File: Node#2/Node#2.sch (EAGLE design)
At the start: 93 parts, among them IC1 TSL25911FN, J1 68712414522, Q1 BC847ALT1SMD, Q2 SI1308EDL-T1-GE3, U2 RV8564C3, U4 TPS63001DRCT

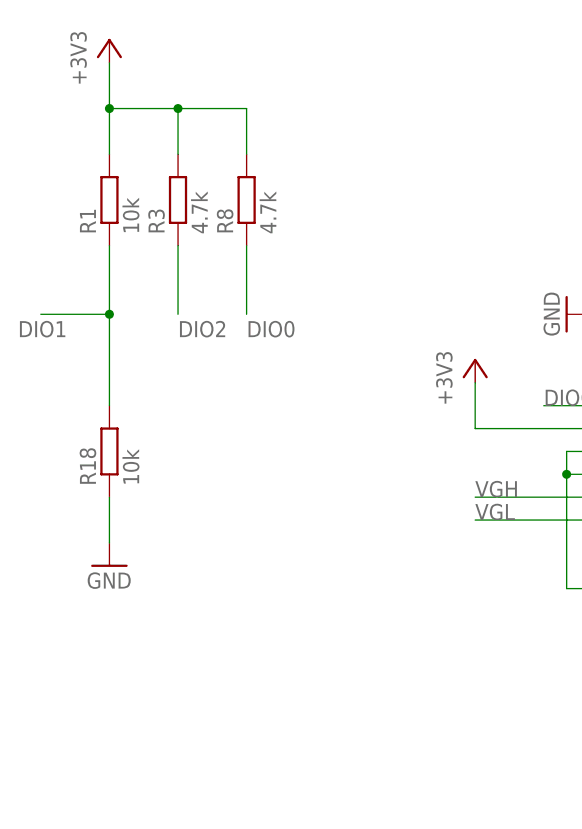
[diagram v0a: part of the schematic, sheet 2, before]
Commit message: Display gedreht, Diodenfootprints
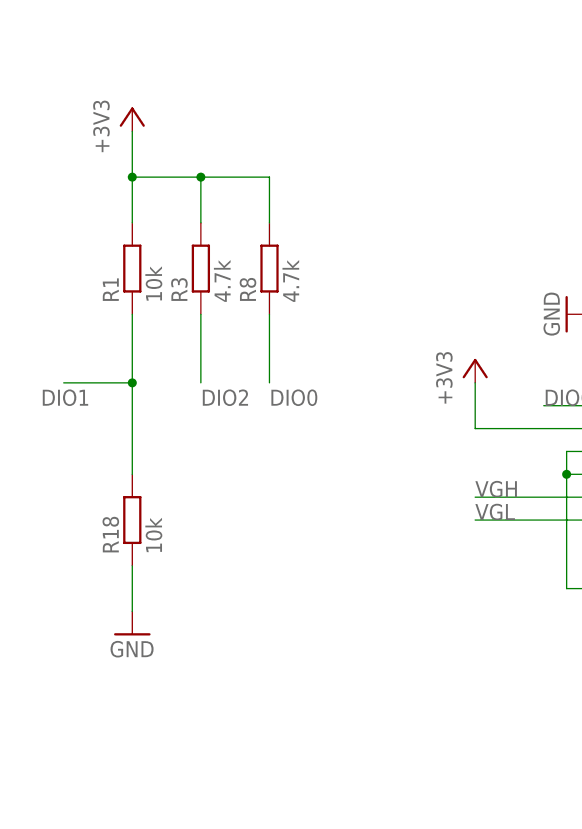
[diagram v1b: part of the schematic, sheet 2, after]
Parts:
- removed !!!FDN304PZ!!!: BSS84, transistor-small-signal:BSS84
- added Q3: FDN304PZ, BlueHome:FDN304PZ
- C1, C19, C2, C20, C21, C22, C23, C24, C25, C26, C27, C28, C29, C30: SPICEPREFIX (none) -> C
- C34: value (none) -> 100n
- D1: value ZPD -> ZENER_SMB; device diode:ZPD -> BlueHome:ZENER_SMB; SPICEPREFIX (none) -> D
- D2: value MUR150RL -> (none); device diode:MUR150RL -> eagle-ltspice:DIODE_E-
- D5, D6, D7: SPICEPREFIX (none) -> D
- J1, U$11: SPICEPREFIX (none) -> X
- Q2: SPICEPREFIX (none) -> Q
- R15, R16: SPICEPREFIX (none) -> R
- R17: value 1.5M -> 3M
- R5: value 1M -> 2M
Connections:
- removed net N$2: D2.A, R2.1
- new net N$1: D2.C, R2.1
- net +3V3_RTC: now also D2.A; no longer D2.C
- net N$14: now also Q3.G; no longer !!!FDN304PZ!!!.G
- net N$8: now also Q3.S; no longer !!!FDN304PZ!!!.S
- net N$9: now also Q3.D; no longer !!!FDN304PZ!!!.D
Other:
- moved on the sheet: R1, R18, R3, R8

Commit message: buttons
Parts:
- added ANT2: CONUFL001-SMD, BlueHome:CONUFL001-SMD
- added C53, C54, C55, C56, C57, C58, C59, C60, C61, C62: (no value), rcl:C-EUC0805K
- added C63, C64, C65, C66, C67, C68: (no value), rcl:C-EUC0805
- added C69, C70: (no value), rcl:C-EUC0402
- added D4: BAS40-06, diode:BAS40-06
- added JMP2: 0R-JUMPA, jump-0r-smd:0R-JUMPA
- added JP3: (no value), pinhead:PINHD-2X5
- added JP5: (no value), jumper:JP1E
- added JP7: (no value), pinhead:PINHD-1X3
- added JP8: (no value), pinhead:PINHD-1X2
- added R30, R31, R32, R33, R36, R37: (no value), rcl:R-EU_R0805
- added R34, R35: (no value), rcl:R-EU_R1210
- added S3, S4: FSM4JSMAATR, BlueHome:FSM4JSMAATR
- added U$15, U$17: L0402, BlueHome:L0402
- added U$16: BALF-NRG-01D3, BlueHome:BALF-NRG-01D3
- added U3: BLUENRG-232, BlueHome:BLUENRG-232
- added Y3: ECS-160-12-36-AGN-TR, BlueHome:ECS-160-12-36-AGN-TR
- added Y4: NX2012SA-32.768K-STD-MUB-1, BlueHome:NX2012SA-32.768K-STD-MUB-1
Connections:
- new net DIO14: C68.1, JP8.1, R34.1, S4.1, S4.2, U3.DIO14/ANATEST0
- new net JTCK: JP3.4, U3.DIO9
- new net JTMS: JP3.2, U3.DIO10
- new net N$47: C59.1, C60.1, U3.VDD1V2
- new net N$48: C61.1, C62.1, JMP2-0R.2, U3.SMPSFILT1
- new net N$49: R31.1, S3.1, S3.2
- new net N$50: C64.1, U3.FXTAL1, Y3.OUT/IN
- new net N$51: C65.2, U3.FXTAL0, Y3.IN/OUT
- new net N$52: C66.2, C67.2, U$15.1
- new net N$53: C66.1, U3.SXTAL0, Y4.2
- new net N$54: C67.1, U3.SXTAL1, Y4.1
- new net N$55: C69.1, U$16.ANT, U$17.1
- new net N$56: ANT2.SIG, C70.1, U$17.2
- new net N$57: JP3.1, JP5.1
- new net N$58: JP8.2, R35.2, S4.3, S4.4
- new net N$59: U$16.RX_P, U3.RF1
- new net N$60: U$16.RX_N, U3.RF0
- new net RXD: JP7.2, U3.DIO11
- new net SMPSFILT2: JMP2-0R.1, U3.SMPSFILT2
- new net TDI: JP3.8, R36.2, U3.DIO0
- new net TDO: JP3.6, R37.2, U3.DIO1
- new net TXD: JP7.1, U3.DIO8
- net +3V3: now also C53.1, C54.1, C55.1, C56.1, C57.1, C58.1, D4.K2, JMP2-0R.3, JP5.2, R30.2, R32.2, R33.2, R34.2, U3.VBAT1, U3.VBAT2, U3.VBAT3
- net ADC1: now also U3.ADC1
- net ADC2: now also U3.ADC2
- net DIO0: now also R36.1
- net DIO1: now also R37.1
- net DIO12: now also U3.DIO12
- net DIO13: now also U3.DIO13
- net DIO2: now also U3.DIO2
- net DIO3: now also U3.DIO3
- net DIO6: now also U3.DIO6
- net DIO7: now also U3.DIO7/BOOT
- net GND: now also ANT2.GND_1, ANT2.GND_2, C53.2, C54.2, C55.2, C56.2, C57.2, C58.2, C59.2, C60.2, C61.2, C62.2, C63.1, C64.2, C65.1, C68.2, C69.2, C70.2, JP3.3, JP3.5, JP3.9, JP7.3, R31.2, R35.1, U$15.2, U$16.GND, U3.EXP, U3.TEST, Y3.GND
- net RESETN: now also C63.2, D4.AA, JP3.10, R30.1, S3.3, S3.4, U3.RESETN
- net SCL: now also R32.1, U3.DIO4
- net SDA: now also R33.1, U3.DIO5
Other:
- note added: "9 IO"
- note added: "ARM 10-PIN Interface"
- note added: "JTAG"
- note added: "Serial"

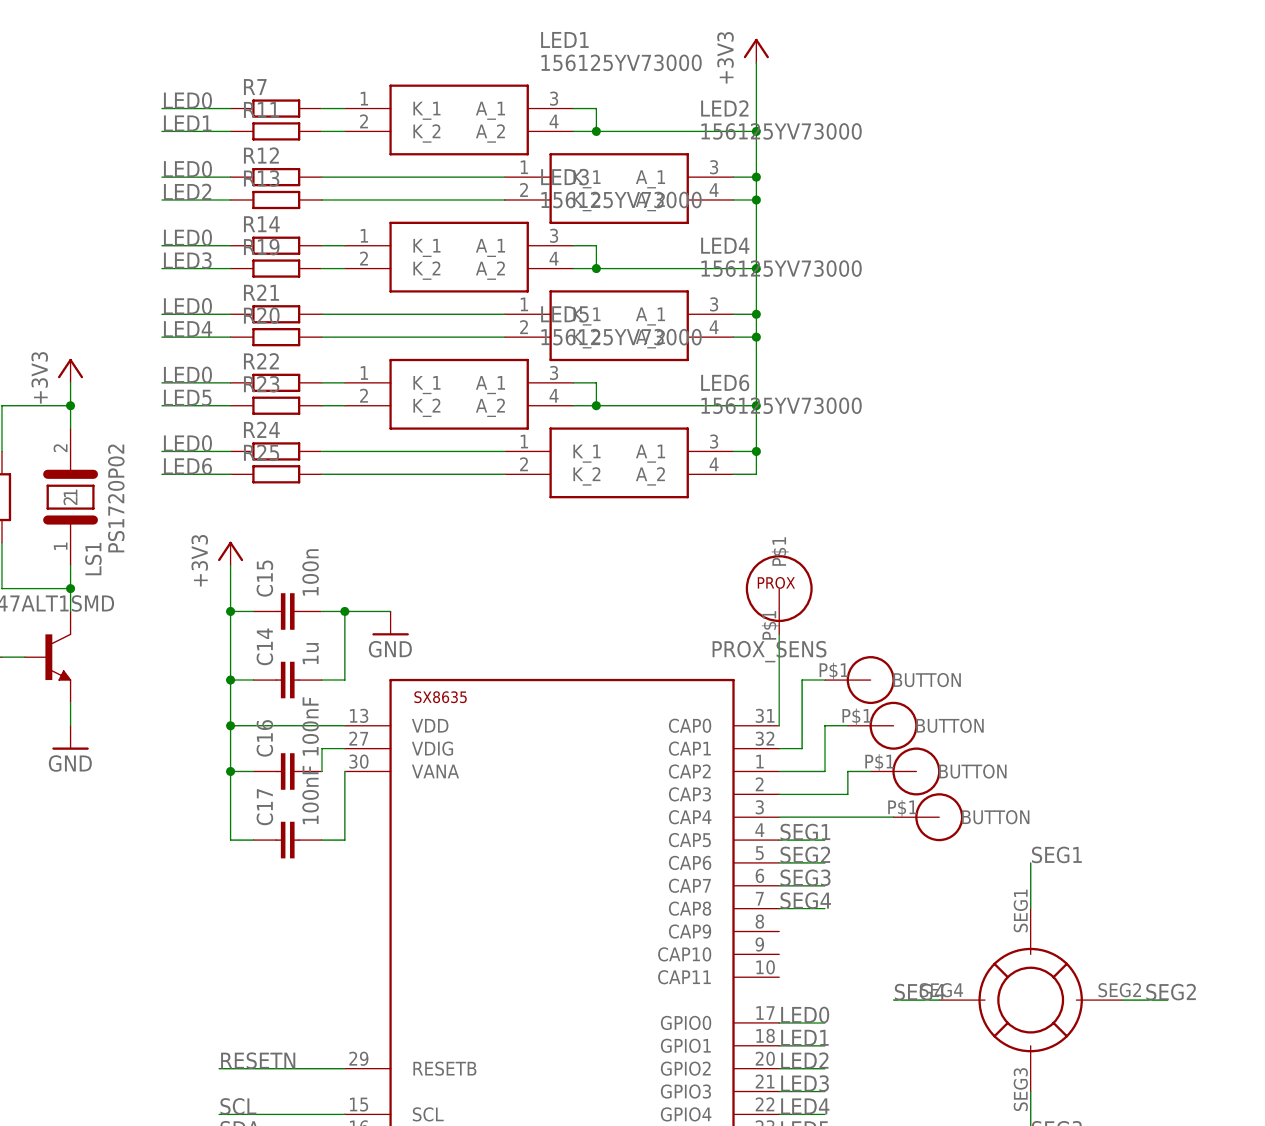
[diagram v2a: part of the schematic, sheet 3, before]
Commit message: Layout: touchbuttons, power
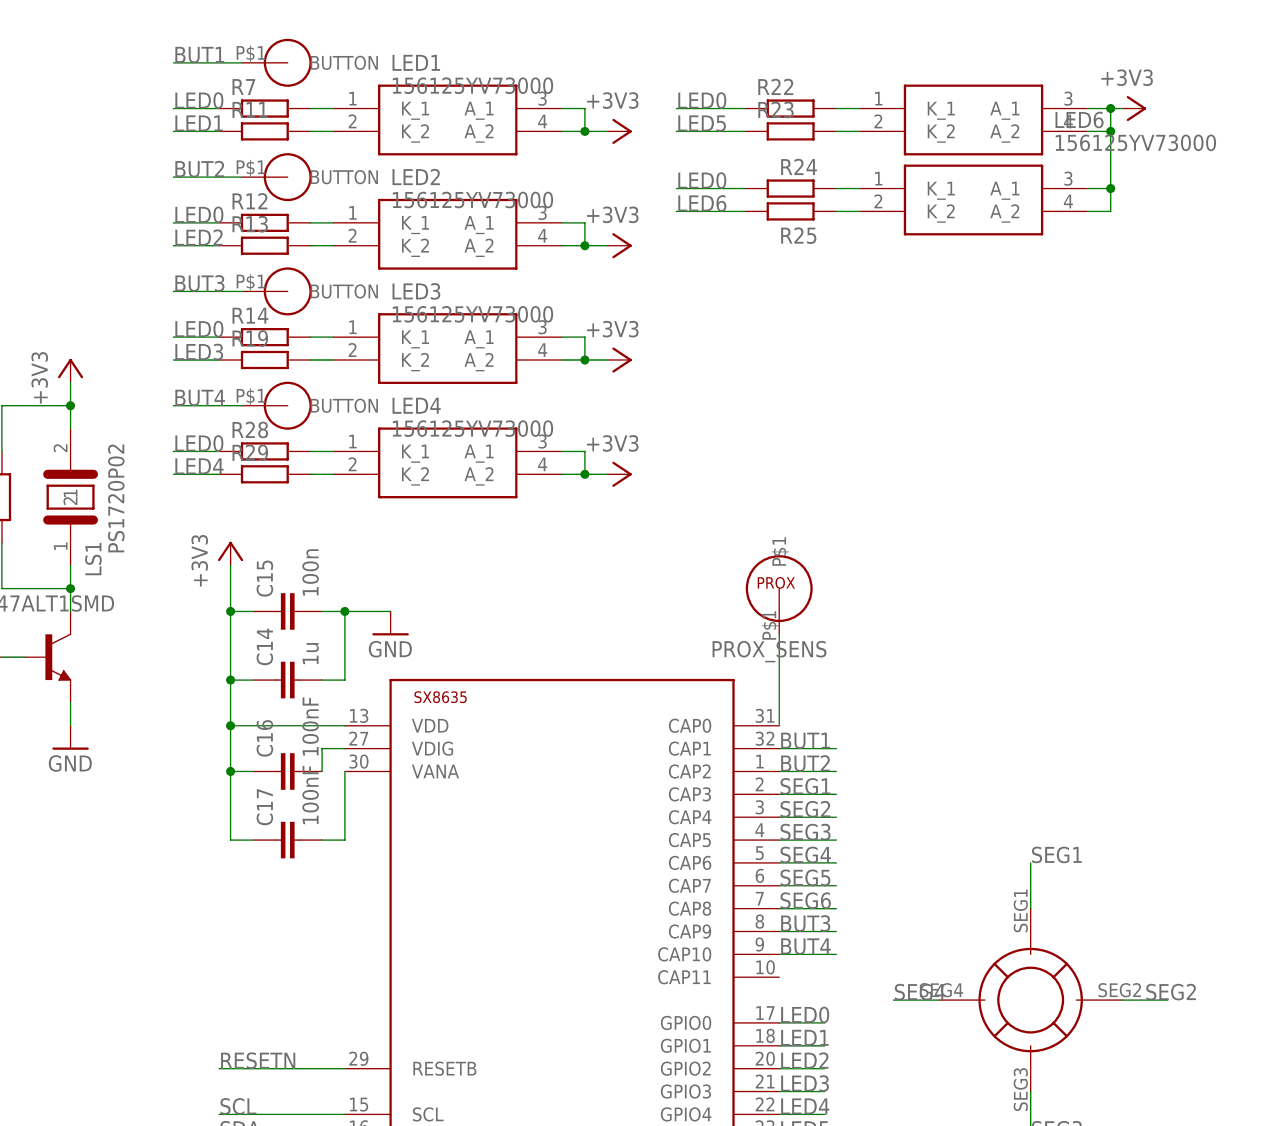
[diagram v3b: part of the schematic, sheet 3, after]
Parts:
- removed R20, R21: (no value), rcl:R-EU_R0805
- removed U$6: TOUCH_BUTTON, BlueHome:TOUCH_BUTTON
- added R28, R29: (no value), rcl:R-EU_R0805
- added U$13: TOUCH_BUTTON, BlueHome:TOUCH_BUTTON
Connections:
- net N$28 renamed BUT1
- net N$29 renamed BUT2
- net N$9 renamed VBAT
- removed net N$27: LED4.K_1, R21.2
- removed net N$32: U$2.CAP4, U$6.BUTTON
- removed net V-: R10.1, U$10.P$2, U4.PGND, U4.POWER_PAD
- new net BUT3: U$2.CAP9, U$5.BUTTON
- new net BUT4: U$13.BUTTON, U$2.CAP10
- new net SEG5: U$2.CAP7
- new net SEG6: U$2.CAP8
- net GND: now also R10.1, U$10.P$2, U4.PGND, U4.POWER_PAD
- net LED0: now also R28.1; no longer R21.1
- net LED4: now also R29.1; no longer R20.1
- net N$30: now also LED4.K_1, R28.2; no longer LED4.K_2, R20.2
- net N$31: now also LED4.K_2, R29.2; no longer U$2.CAP3, U$5.BUTTON
- net SEG1: now also U$2.CAP3; no longer U$2.CAP5
- net SEG2: now also U$2.CAP4; no longer U$2.CAP6
- net SEG3: now also U$2.CAP5; no longer U$2.CAP7
- net SEG4: now also U$2.CAP6; no longer U$2.CAP8
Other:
- moved on the sheet: LED1, LED2, LED3, LED4, LED6, R11, R12, R13, R14, R19, R22, R23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

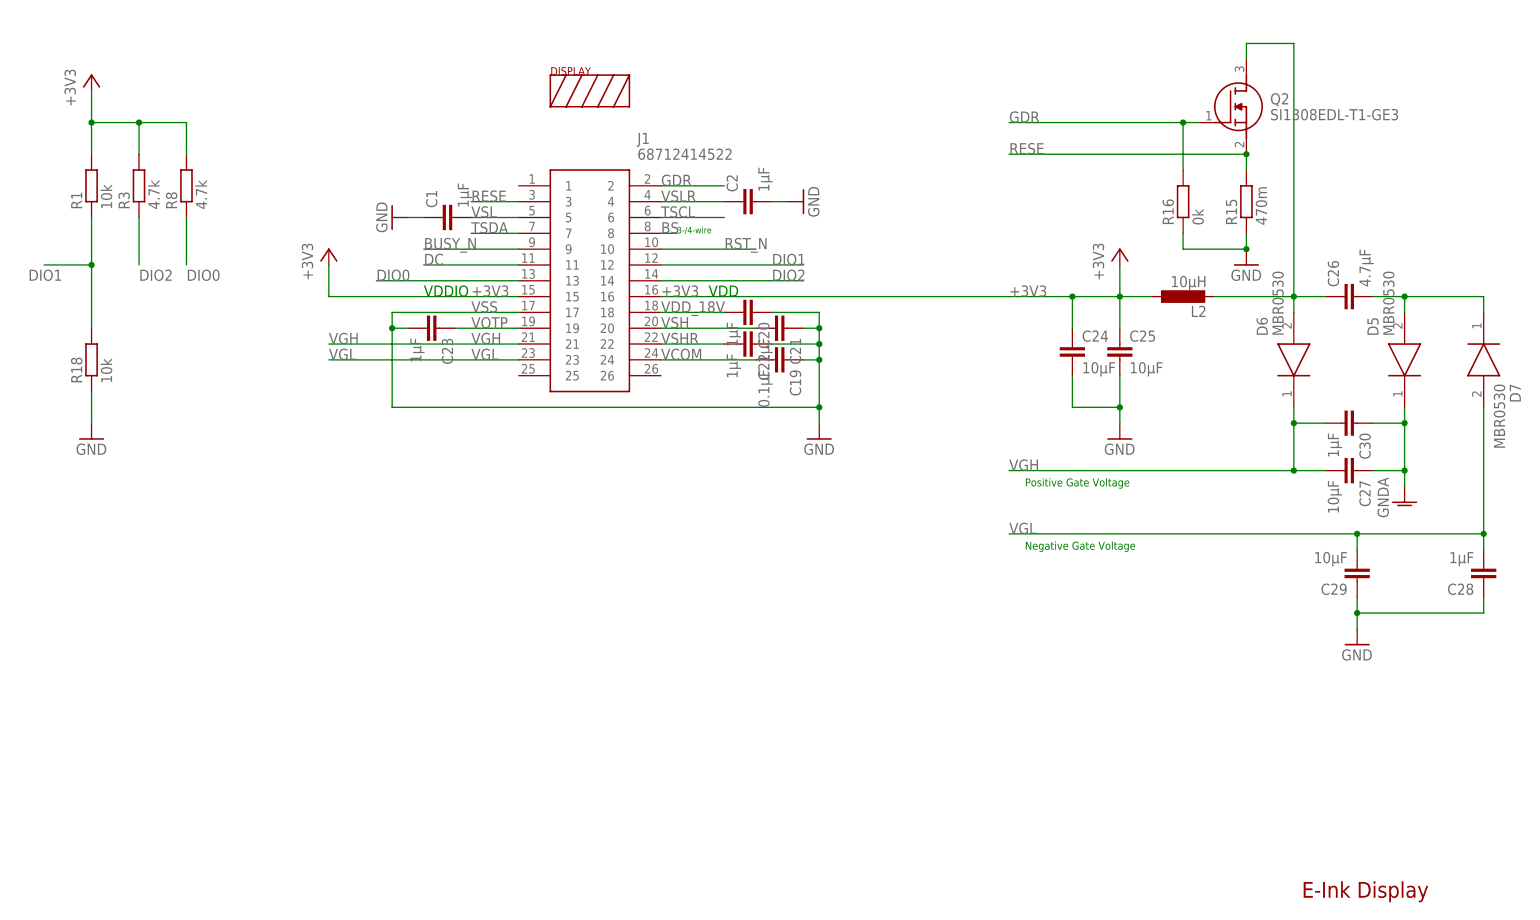
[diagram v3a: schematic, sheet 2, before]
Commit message: Resolve Merge Error in Lib
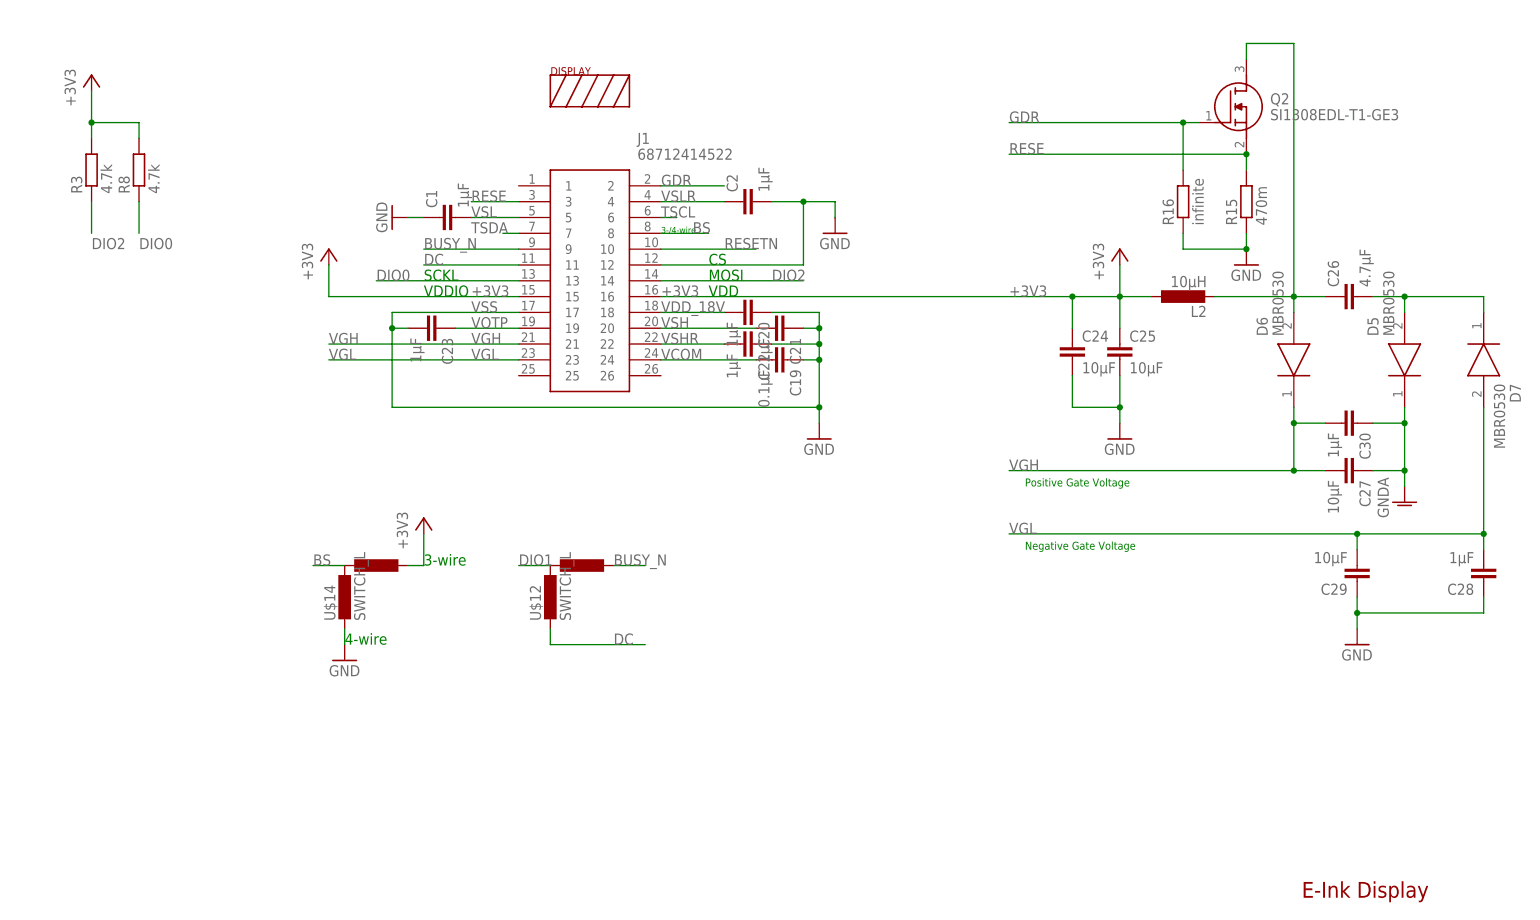
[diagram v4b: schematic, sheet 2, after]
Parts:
- removed R1, R18: 10k, rcl:R-EU_R0805
- added U$12, U$14, U$6: SWITCH_L, BlueHome:SWITCH_L
- R16: value 0k -> infinite
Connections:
- net N$10 renamed L1
- net N$11 renamed L2
- removed net RST_N: J1.10
- new net PS: U$6.2, U4.PS/SYNC
- net +3V3: now also U$14.3; no longer R1.2
- net BS: now also U$14.1
- net BUSY_N: now also U$12.3
- net DC: now also U$12.2
- net DIO1: now also U$12.1; no longer J1.12, R1.1, R18.2
- net GND: now also J1.12, U$14.2, U$6.1; no longer R18.1
- net N$12: now also U$6.3; no longer U4.PS/SYNC
- net RESETN: now also J1.10
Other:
- note added: "3-wire"
- note added: "4-wire"
- note added: "CS"
- note added: "MOSI"
- note added: "SCKL"
- moved on the sheet: R3, R8

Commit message: display
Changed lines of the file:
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@@
 <?xml version="1.0" encoding="utf-8"?>
 <!DOCTYPE eagle SYSTEM "eagle.dtd">
-<eagle version="9.3.0">
+<eagle version="9.2.1">
 <drawing>
 <settings>
@@
 <part name="C34" library="rcl" deviceset="C-EU" device="C0805" value="100n"/>
 <part name="LS1" library="BlueHome" deviceset="PS1720P02" device=""/>
-<part name="Q1" library="transistor-npn" library_urn="urn:adsk.eagle:library:398" deviceset="BC847*" device="SMD" package3d_urn="urn:adsk.eagle:package:28738/2" technology="ALT1"/>
+<part name="Q1" library="transistor-npn" library_urn="urn:adsk.eagle:library:398" deviceset="BC847*" device="SMD" package3d_urn="urn:adsk.eagle:package:28984/2" technology="ALT1"/>
 <part name="R4" library="rcl" deviceset="R-EU_" device="R0805"/>
 <part name="R6" library="rcl" deviceset="R-EU_" device="R0805"/>
